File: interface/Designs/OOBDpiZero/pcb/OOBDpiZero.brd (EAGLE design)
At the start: 73.5 x 42 mm, 132 parts, among them IC1 LM1117MPX-3.3, IC11 EEPROM24, IC3 DS3231, Q2 12MHz, U1 SN65HVD230(SO8), U2 SN65HVD230(SO8), U3 MAX98357, U4 SY6280, U5 MP1482

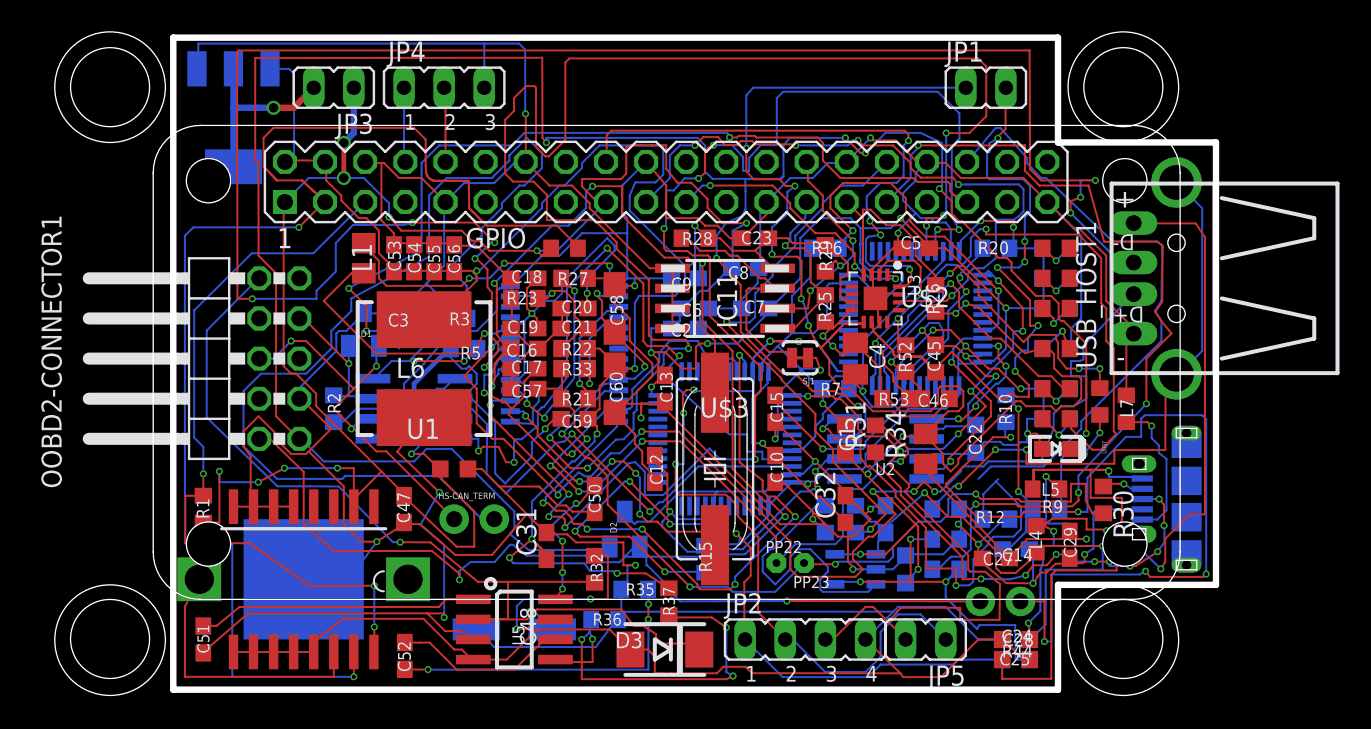
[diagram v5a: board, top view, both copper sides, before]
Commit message: start modifications on wire width to a default of 10mil modify all via to octagon instead of mixture for round a square
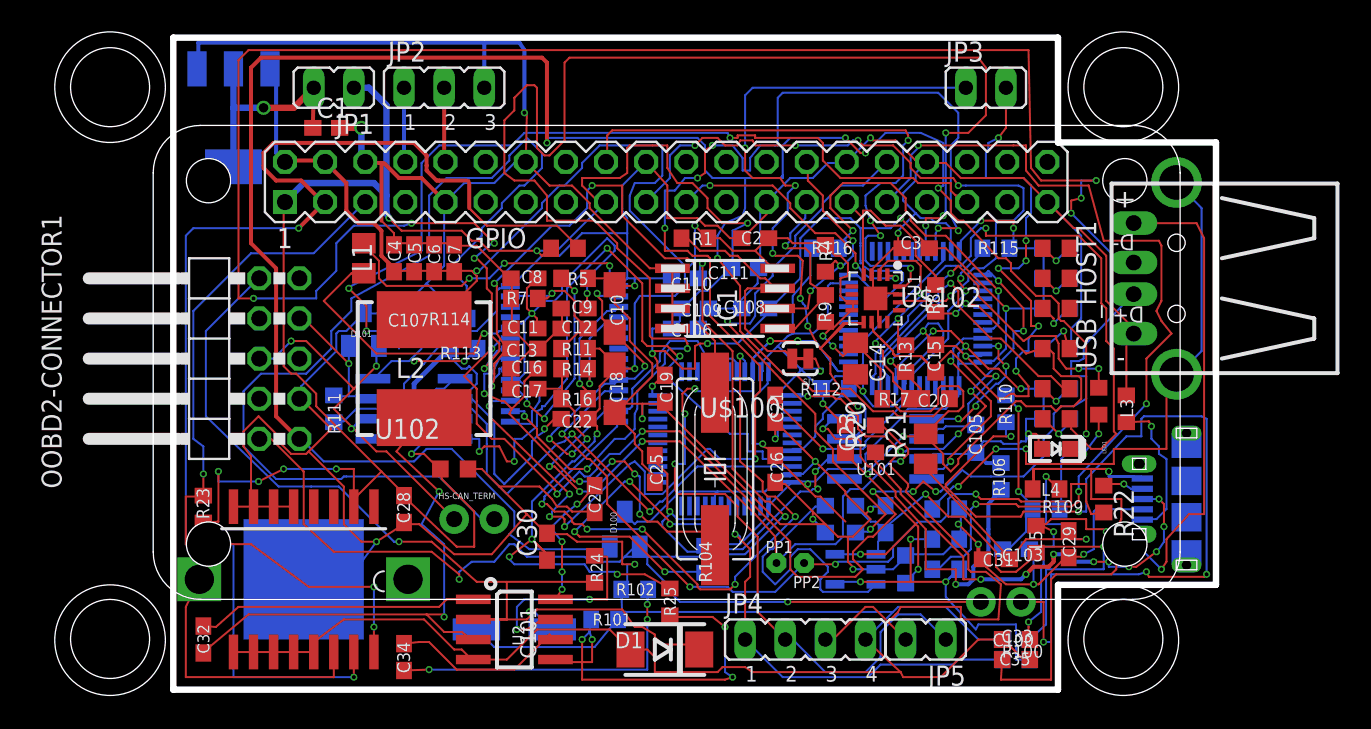
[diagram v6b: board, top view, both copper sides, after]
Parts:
- removed C45, C46: 220pF, rcl:C0603K
- removed C47: 1uF, rcl:C0603
- removed C50: 100nF, rcl:C0603
- removed C51: 10nF, rcl:C0603
- removed C52: 3.3nF, rcl:C0603
- removed C53, C54, C55, C56: 22uF/6.3V, rcl:C0603
- removed C57, C59: 100nF, resistor:C0603
- removed C58, C60: 22uF/6.3V, rcl:SMC_A
- removed D3: SMBJ16A, OLIMEX_DISCRET:DO214AA
- removed IC11: EEPROM24, FLYFISH:SOIC8
- removed L7: FB0805/600R/2A, rcl:L0603
- removed R26: 1M, resistor:R0603
- removed R27: 680R, resistor:R0603
- removed R28, R32: 10k, rcl:R0603
- removed R30, R31: NI(0R), resistor:R0603
- removed R33: 10k, resistor:R0603
- removed R34: NI(0R), resistor:R0805
- removed R37: 4.99k/1%, rcl:R0603
- removed R39: 2.2k/1%, rcl:R0603
- removed R52, R53: NI, resistor:R0603
- removed U3: MAX98357, microbuilder:QFN16_3MM
- removed U5: MP1482, OLIMEX_IC:SOIC8
- added C100, C104: 22uF/6.3V, rcl:C0603
- added C102, C105, C33, C35: 100nF, rcl:C0603K
- added C103, C107: NI (10nF), resistor:C0603
- added C106, C108, C109, C110, C111: 100nF, resistor:C0603
- added C34: 3.3nF, rcl:C0603
- added D101: PESD1CAN, Industrialberry:SOT23
- added IC100: LM1117MPX-3.3, lm1117:SOT223
- added L100: FB0805/600R/2A, rcl:L0603
- added R104, R115: 330R, rcl:R0603
- added R106, R113: 10k, rcl:R0603
- added R108: 6k8k/1%, rcl:R0603
- added R109, R110, R111, R112, R114, R116: 60R, resistor:R0603
- added R11: 10k, resistor:R0603
- added U101, U102: SN65HVD230(SO8), arm:SO-08
- C1, C30: value 100nF -> 10uF/6.3V; device rcl:C0603K -> rcl:C0603
- C10, C18: value 100nF -> 22uF/6.3V; device resistor:C0603 -> rcl:SMC_A
- C11, C22, C25: device rcl:C0603K -> resistor:C0603
- C12: value 100nF -> 1uF
- C13: value 100nF -> 33pF
- C14: value NI (10nF) -> 10uF; device resistor:C0603 -> rcl:C0805K
- C15, C20: value 100nF -> 220pF; device resistor:C0603 -> rcl:C0603K
- C17: value 33pF -> 100nF
- C2: device resistor:C0603 -> rcl:C0603
- C21: value 1uF -> 100nF
- C23: device rcl:C0603 -> rcl:C0603K
- C26: value 22uF/6.3V -> 100nF; device rcl:C0603 -> resistor:C0603
- C27: value 22uF/6.3V -> 100nF
- C28: value 22uF/6.3V -> 1uF
- C3: value NI (10nF) -> 100nF
- C31: value 10uF/6.3V -> 22uF/6.3V
- C32: value 10uF/6.3V -> 10nF
- C4: value 10uF -> 22uF/6.3V; device rcl:C0805K -> rcl:C0603
- C5, C6, C7: value 100nF -> 22uF/6.3V; device resistor:C0603 -> rcl:C0603
- D1: value PESD1CAN -> SMBJ16A; device Industrialberry:SOT23 -> OLIMEX_DISCRET:DO214AA
- IC1: value LM1117MPX-3.3 -> EEPROM24; device lm1117:SOT223 -> FLYFISH:SOIC8
- JP1: value Audio-Out -> 3V3 power (opt)
- JP2: value Prog0_IO -> UART; device jumper:JP4 -> jumper:JP2
- JP3: value 3V3 power (opt) -> Audio-Out
- JP4: value UART -> Prog0_IO; device jumper:JP2 -> jumper:JP4
- R10, R3: value 60R -> 330R; device resistor:R0603 -> rcl:R0603
- R12: value 10k -> 2.2k/1%
- R13, R17: value 330R -> NI; device rcl:R0603 -> resistor:R0603
- R14: value 330R -> 10k; device rcl:R0603 -> resistor:R0603
- R16: value 60R -> 10k
- R2, R9: value 60R -> 10k; device resistor:R0603 -> rcl:R0603
- R20: value 330R -> NI(0R); device rcl:R0603 -> resistor:R0603
- R21: value 10k -> NI(0R); device resistor:R0603 -> resistor:R0805
- R22: value 10k -> NI(0R)
- R23: value NA(47k) -> 10k; device resistor:R0603 -> rcl:R0603
- R24: value 6k8k/1% -> 10k
- R25: value 10k -> 4.99k/1%
- R5: value 10k -> 680R; device rcl:R0603 -> resistor:R0603
- R6: value 10k -> 330R
- R7: value 60R -> NA(47k)
- R8: value 330R -> 1M; device rcl:R0603 -> resistor:R0603
- U1: value SN65HVD230(SO8) -> MAX98357; device arm:SO-08 -> microbuilder:QFN16_3MM
- U2: value SN65HVD230(SO8) -> MP1482; device arm:SO-08 -> OLIMEX_IC:SOIC8
- moved JP2 41.7 mm to (17.1, 37.5)
- moved JP4 41.7 mm to (40.0, 2.54)
- moved C32 41.5 mm to (1.91, 2.54), turned to 270 degrees
- moved JP1 41.3 mm to (10.2, 37.5), turned to 90 degrees
- moved JP3 41.3 mm to (51.4, 37.5), turned to 270 degrees
- moved C28 39.6 mm to (14.6, 10.8), flipped to the top, turned to 90 degrees
- moved R3 38.4 mm to (55.9, 27.3), flipped to the top, turned to 0 degrees
- moved C1 38.3 mm to (9.68, 34.9), turned to 0 degrees
- moved C24 37.2 mm to (17.8, 13.3), turned to 0 degrees
- moved R1 35.5 mm to (33.0, 27.9), turned to 180 degrees
- moved R22 34.8 mm to (58.9, 11.4), turned to 270 degrees
- moved IC1 33.1 mm to (34.9, 24.1), flipped to the top, turned to 270 degrees
- moved C3 32.7 mm to (47.0, 27.3), flipped to the top
- moved C5 31.8 mm to (15.2, 26.7), turned to 90 degrees
- moved R14 31.4 mm to (25.4, 19.7), turned to 180 degrees
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- renumbered BAT1 to BAT100, C48 to C101, D2 to D100, IC3 to IC2, L6 to L2, LED3 to LED103, LED4 to LED102, LED5 to LED104, LED6 to LED101, LED7 to LED1, LED8 to LED100, PP22 to PP1, PP23 to PP2, Q2 to Q1, R29 to R4, R35 to R102, R36 to R101, R41 to R105, R42 to R107, R43 to R103, R44 to R100, U$2 to U$102, U$3 to U$100, U$5 to U$101, U4 to U100, USB_HOST2 to USB_HOST100
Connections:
- net +12V: now also D1.C, R24.1, U2.2; no longer D3.C, R32.1, U5.2
- net +3V3: now also C105.1, C106.2, C108.2, C109.2, C111.2, C19.2, C24.1, C25.2, C26.2, C28.2, C3.2, JP1.1, JP4.1, R104.1, R106.2, R113.2, R115.1, R2.1, R23.1, U101.3, U102.3; no longer C10.2, C11.1, C12.2, C13.2, C2.2, C22.1, C47.2, C5.2, C6.2, C7.2, C8.2, JP2.1, JP3.1, R1.1, R12.2, R15.1, R20.1, R5.2, R6.1, U1.3, U2.3
- net +5V: now also C102.1, C14.1, C18.+, C2.2, C22.1, C23.1, C5.1, C6.1, C7.1, IC1.8, IC100.3, R1.1, R11.1, R12.1, R17.2, R21.2, R25.2, R8.2, R9.1, U1.7, U1.8; no longer C1.1, C23.2, C31.1, C53.1, C54.1, C55.1, C56.1, C59.1, C60.+, IC1.3, IC11.8, R22.1, R25.1, R26.2, R28.1, R34.2, R37.2, R39.1, R53.2, U3.7, U3.8
- net AUD_BCLK: now also U1.16; no longer U3.16
- net AUD_DIN: now also U1.1; no longer U3.1
- net AUD_LRCLK: now also U1.14; no longer U3.14
- net AUD_SD_MODE: now also R8.1, U1.4; no longer R26.1, U3.4
- net GND: now also C10.-, C100.2, C102.2, C103.2, C104.2, C105.2, C106.1, C107.2, C108.1, C109.1, C110.1, C111.1, C12.2, C13.2, C18.-, C19.1, C20.1, C21.1, C23.2, C25.1, C26.1, C28.1, C3.1, C33.2, C35.2, C5.2, C6.2, C7.2, C8.2, C9.2, D1.A, D101.3, IC1.2, IC1.3, IC1.4, IC100.1, JP2.3, JP4.4, L100.1, R108.1, R112.2, R116.2, R13.1, R5.1, R7.1, U1.11, U1.15, U1.3, U1.THERMAL, U101.2, U102.2, U2.4; no longer C10.1, C12.1, C13.1, C18.2, C19.2, C20.2, C21.2, C23.1, C25.2, C26.2, C28.2, C3.2, C32.2, C45.1, C46.1, C47.1, C5.1, C50.2, C53.2, C54.2, C55.2, C56.2, C57.2, C58.-, C59.2, C6.1, C60.-, C7.1, C8.1, C9.1, D1.3, D3.A, IC11.1, IC11.2, IC11.3, IC11.4, JP2.4, JP4.3, L7.1, R16.2, R23.1, R24.1, R27.1, R52.1, R7.2, U1.2, U2.2, U3.11, U3.15, U3.3, U3.THERMAL, U5.4
- net HS-CAN_H: now also D101.2, R111.2, U102.7; no longer D1.2, R2.2, U1.7
- net HS-CAN_L: now also D101.1, U102.6; no longer D1.1, U1.6
- net HS-CAN_RXD: now also U102.4; no longer U1.4
- net HS-CAN_TXD: now also U102.1; no longer U1.1
- net ID_SC: now also IC1.6; no longer IC11.6
- net ID_SD: now also IC1.5, R9.2; no longer IC11.5, R25.2
- net MS-CAN_H: now also R109.2, U101.7; no longer R9.2, U2.7
- net MS-CAN_L: now also U101.6; no longer U2.6
- net MS-CAN_RXD: now also U101.4; no longer U2.4
- net MS-CAN_TXD: now also U101.1; no longer U2.1
- net N$1: now also C31.1, L4.1, R21.1; no longer C27.1, L5.1, R34.1
- net N$10: now also C103.1, R109.1, R110.1; no longer C14.1, R10.1, R9.1
- net N$11: now also C34.2; no longer C52.2
- net N$12: now also C20.2, JP3.1, U1.9; no longer C46.2, JP1.1, U3.9
- net N$129: now also R12.2; no longer R39.2
- net N$13: now also R6.2; no longer R8.2
- net N$14: now also R10.2; no longer R13.2
- net N$15: now also R112.1; no longer R7.1
- net N$16: now also R3.2; no longer R14.2
- net N$17: now also R3.1; no longer R14.1
- net N$18: now also R10.1; no longer R13.1
- net N$19: now also R6.1; no longer R8.1
- net N$2: now also C107.1, R111.1, R114.1; no longer C3.1, R2.1, R3.1
- net N$20: now also C110.2, R104.2; no longer C9.2, R15.2
- net N$21: now also R116.1; no longer R16.1
- net N$22: now also R15.2; no longer R17.2
- net N$27: now also R15.1; no longer R17.1
- net N$28: now also C21.2, R115.2; no longer C15.2, R20.2
- net N$29: now also C16.1; no longer C17.1
- net N$3: now also C15.2, JP3.2, U1.10; no longer C45.2, JP1.2, U3.10
- net N$30: now also R114.2; no longer R3.2
- net N$31: now also C13.1; no longer C16.1
- net N$32: now also R110.2; no longer R10.2
- net N$33: now also C10.+, C17.1, R14.2, R16.2; no longer C57.1, C58.+, R21.2, R33.2
- net N$34: now also R14.1; no longer R33.1
- net N$35: now also R16.1; no longer R21.1
- net N$36: now also C12.1, R11.2, R7.2; no longer C21.1, R22.2, R23.2
- net N$37: now also R13.2, R17.1, U1.2; no longer R52.2, R53.1, U3.2
- net N$38: now also R22.1; no longer R30.1
- net N$39: now also C11.1, C8.1, C9.1; no longer C18.1, C19.1, C20.1
- net N$4: now also C27.1, U2.8; no longer C50.1, U5.8
- net N$40: now also R5.2; no longer R27.2
- net N$41: now also C33.1, L5.2; no longer C24.1, L4.2
- net N$42: now also L100.2; no longer L3.2
- net N$43: now also R20.1; no longer R31.1
- net N$44: now also L3.2; no longer L7.2
- net N$45: now also R108.2; no longer R24.2
- net N$46: now also IC1.7, R1.2; no longer IC11.7, R28.2
- net N$47: now also C100.1, C104.1, L5.1; no longer C26.1, C28.1, L4.1
- net N$48: now also C35.1, L4.2; no longer C25.1, L5.2
- net N$5: now also R113.1, U102.8; no longer R5.1, U1.8
- net N$50: now also C1.1, IC100.2, IC100.TAB, JP1.2; no longer C32.1, IC1.2, IC1.TAB, JP3.2
- net N$6: now also R24.2, U2.7; no longer R32.2, U5.7
- net N$62: now also R25.1, U2.5; no longer R37.1, U5.5
- net N$7: now also C32.1, U2.1; no longer C51.1, U5.1
- net N$8: now also C32.2, U2.3; no longer C51.2, U5.3
- net N$80: now also R106.1, U101.8; no longer R12.1, U2.8
- net N$9: now also C34.1, U2.6; no longer C52.1, U5.6
- net PP22: now also R20.2; no longer R31.2
- net PP23: now also R22.2; no longer R30.2
- net SCL: now also R23.2; no longer R1.2
- net SDA: now also R2.2; no longer R6.2
- net SWCLK: now also JP4.3; no longer JP2.3
- net SWDIO: now also JP4.2; no longer JP2.2
- net UART0_RXD: now also JP2.2; no longer JP4.2
- net UART0_TXD: now also JP2.1; no longer JP4.1
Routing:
- net MS-CAN_RS: track 38.4 -> 0.00 mm
- net N$80: track 30.5 -> 24.7 mm
- net SDA: track 91.2 -> 86.8 mm
- net +3V3: track 297.4 -> 301.2 mm, vias 25 -> 23
- net N$50: track 11.8 -> 14.3 mm
- net +5V: track 191.0 -> 190.0 mm
- net GND: track 592.0 -> 592.9 mm, vias 24 -> 25
- net N$43: track 29.0 -> 29.8 mm

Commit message: 83 remaining DRC, Mike please take a look.
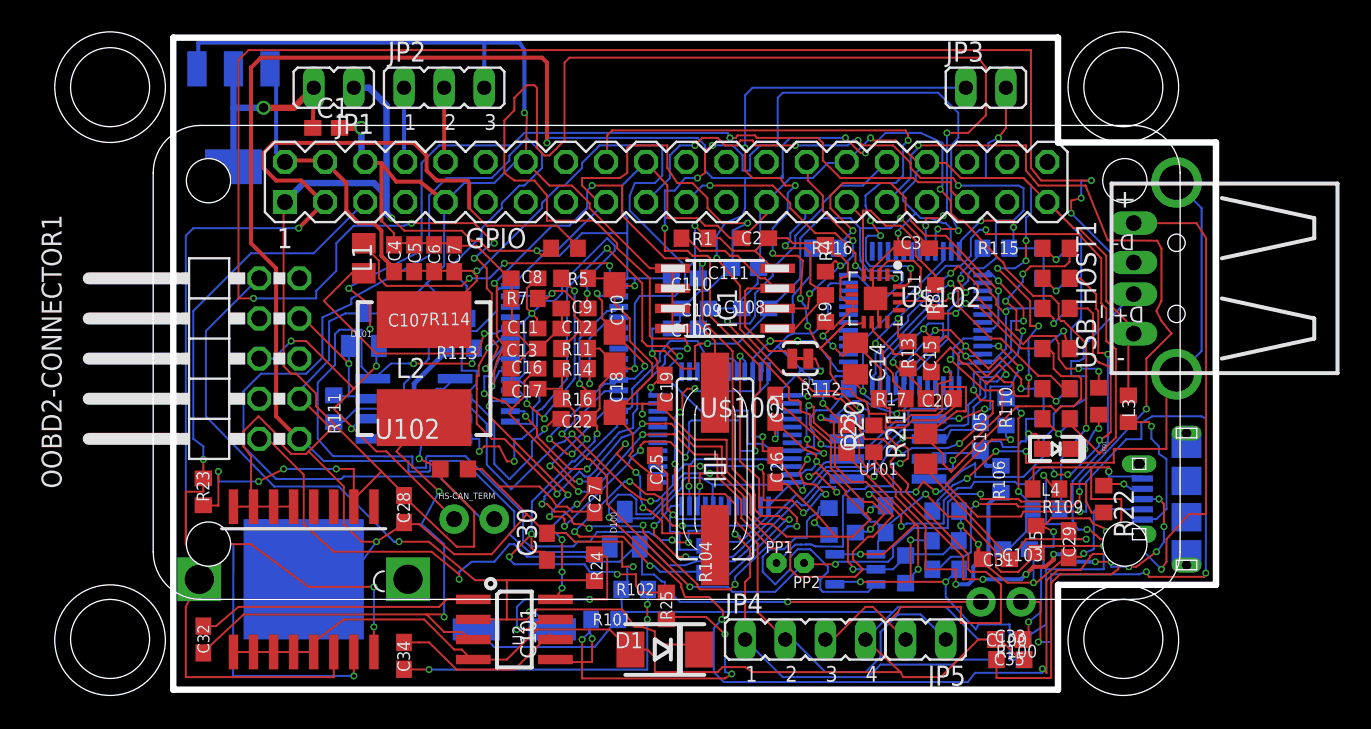
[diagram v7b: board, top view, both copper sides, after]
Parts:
- moved R23 1.09 mm to (1.91, 11.9)
- moved C100 0.43 mm to (52.9, 2.54)
- moved C33 0.43 mm to (52.9, 2.54)
- moved R100 0.38 mm to (53.0, 1.27)
- moved C35 0.36 mm to (53.0, 1.27)
- moved R25 0.34 mm to (31.2, 4.67)
- moved C105 0.31 mm to (51.1, 15.4)
- moved C15 0.28 mm to (48.0, 20.3)
- moved R108 0.27 mm to (41.5, 10.0)
- moved R13 0.27 mm to (46.5, 20.5)
- moved C20 0.25 mm to (48.5, 17.8)
- moved R113 0.23 mm to (18.2, 21.0)
- moved R110 0.20 mm to (52.7, 16.9)
- moved R17 0.20 mm to (45.5, 17.8)
- moved R106 0.18 mm to (52.4, 12.7)
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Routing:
- net N$13: track 0.00 -> 81.0 mm, vias 0 -> 7
- net N$14: track 0.00 -> 60.6 mm, vias 0 -> 13
- net N$5: track 8.44 -> 55.8 mm, vias 2 -> 4
- net N$16: track 0.00 -> 44.1 mm, vias 0 -> 5
- net N$80: track 24.7 -> 37.8 mm, vias 2 -> 4
- net SWDIO: track 67.3 -> 59.2 mm
- net N$48: track 41.3 -> 33.4 mm
- net SDA: track 86.8 -> 80.4 mm
- net GND: track 592.9 -> 598.2 mm
- net N$3: track 46.2 -> 41.4 mm
- net MS-CAN_L: track 72.0 -> 76.6 mm
- net PP22: track 42.4 -> 45.5 mm
- net HS-CAN_RS: track 55.6 -> 52.8 mm
- net N$29: track 28.2 -> 30.7 mm
- net USB2_DP: track 75.3 -> 77.7 mm
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
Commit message: - DRC with "PCB-POOL HighSpec.dru" without errors - One signal "SDIO" not routed completely
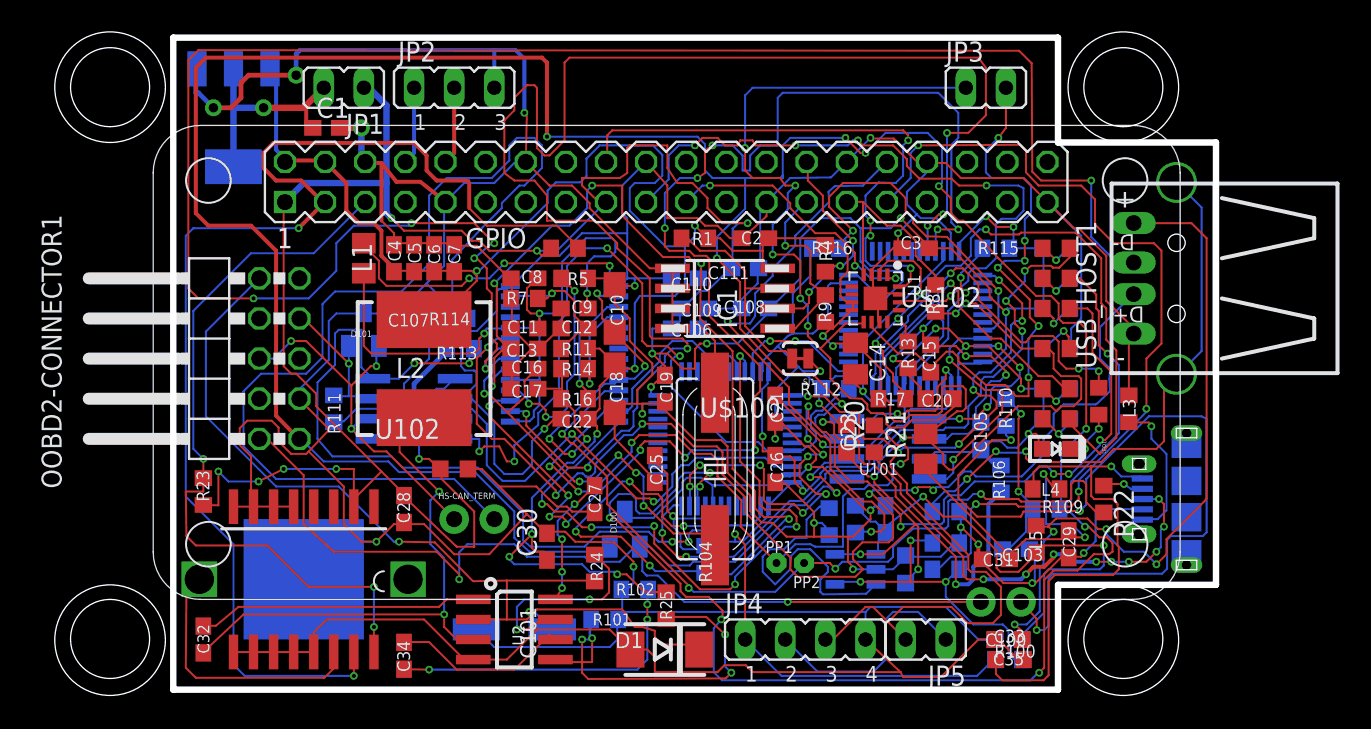
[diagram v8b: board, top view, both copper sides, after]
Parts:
- GPIO: value PIZERO_THROUGH_HOLE -> OOBDpiZero
- moved JP2 0.64 mm to (17.8, 37.5)
- moved JP1 0.63 mm to (10.8, 37.5)
- moved R105 0.14 mm to (48.9, 8.65)
- moved R100 0.10 mm to (52.9, 1.27)
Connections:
- removed net HS-CAN_RS: GPIO.35
- removed net MS-CAN_RS: GPIO.36
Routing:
- net HS-CAN_RS: track 52.8 -> 0.00 mm, vias 3 -> 0
- net SWDIO: track 59.2 -> 33.4 mm, vias 7 -> 2
- net +3V3: track 299.9 -> 293.3 mm
- net MS-CAN_H: track 157.9 -> 163.0 mm
- net N$32: track 57.2 -> 52.4 mm, vias 5 -> 3
- net USB1_DP: track 89.3 -> 84.7 mm
- net USB2_DM: track 117.3 -> 121.3 mm, vias 8 -> 6
- net N$80: track 37.8 -> 34.0 mm
- net N$12: track 54.2 -> 51.7 mm
- net N$3: track 41.4 -> 39.2 mm
- net SDA: track 80.4 -> 78.2 mm
- net N$29: track 30.7 -> 28.6 mm
- net N$48: track 33.4 -> 31.6 mm, vias 2 -> 1
- net N$39: track 45.9 -> 47.5 mm
- net N$5: track 55.8 -> 54.4 mm
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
